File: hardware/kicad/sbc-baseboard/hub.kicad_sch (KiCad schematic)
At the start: 84 parts, among them J1 USB-C upstream, J4 USB-A x2, J5 USB-A x2, U401 USBLC6-2SC6, U402 USB2517, U403 TPS2553DBV, U404 TPS2553DBV, U405 TPS2553DBV, U406 TPS2553DBV, U407 TPS2553DBV, U408 USBLC6-2SC6, U409 USBLC6-2SC6, U410 USBLC6-2SC6, U411 USBLC6-2SC6, Y401 24MHz

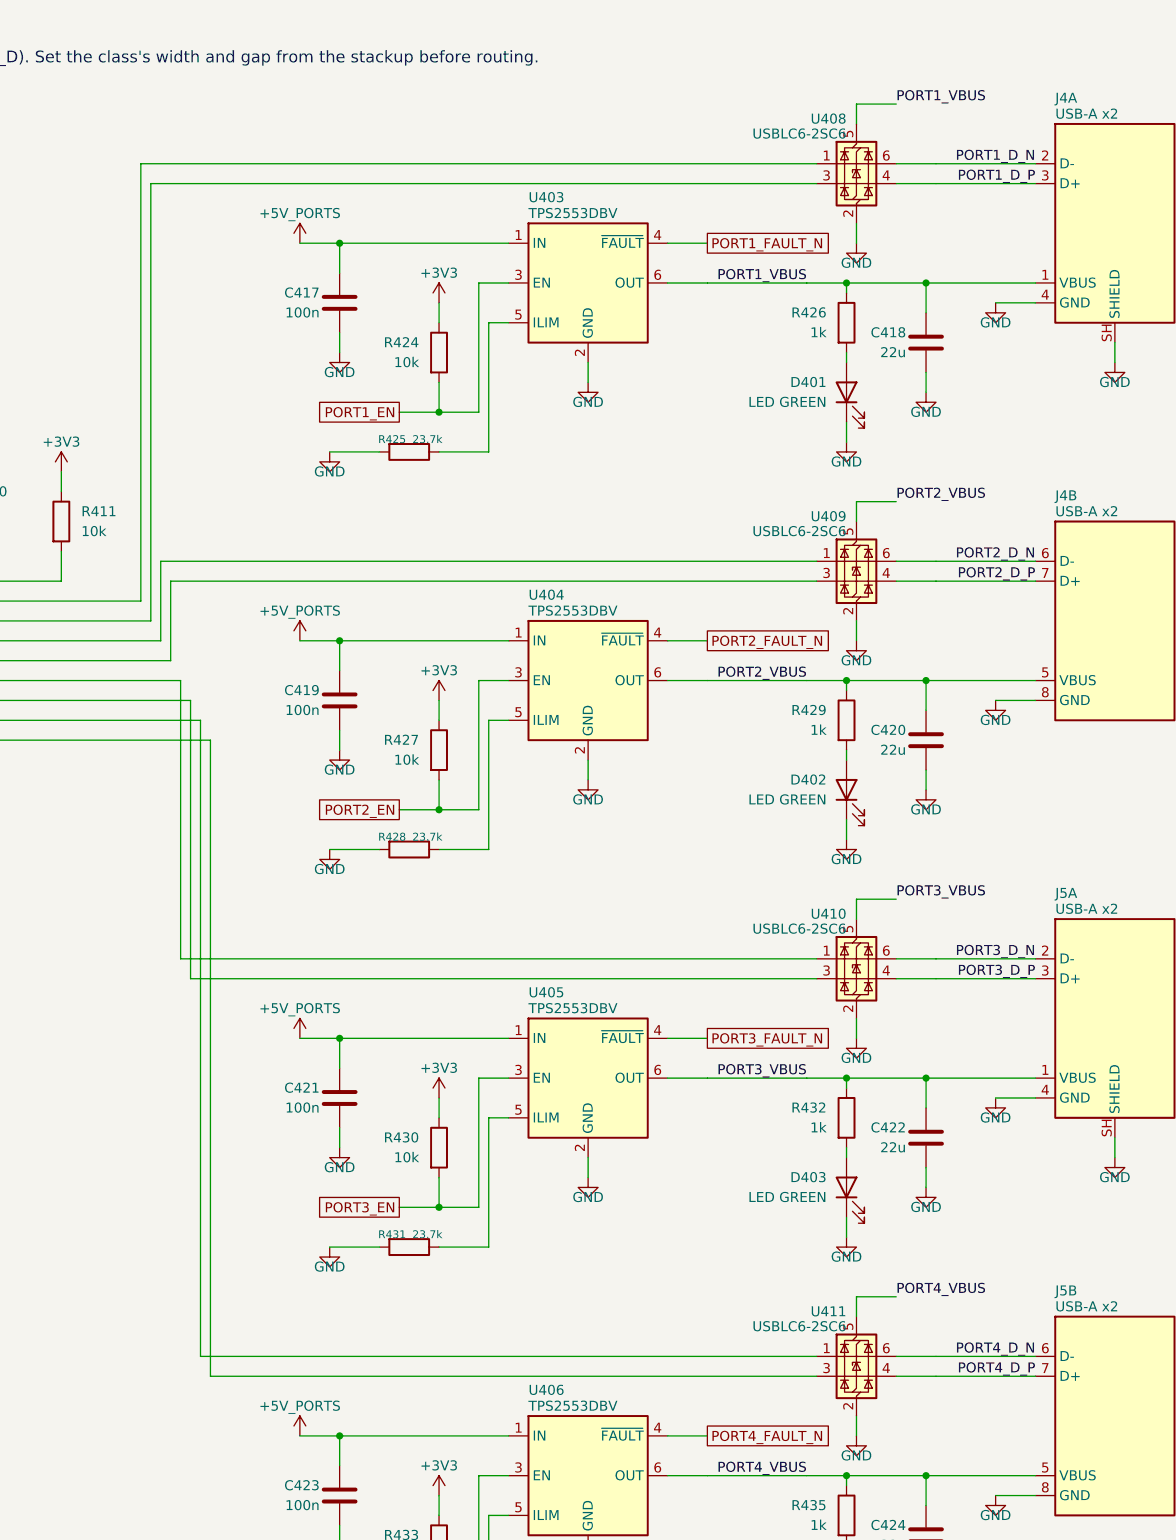
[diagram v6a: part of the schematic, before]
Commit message: Pairs laid as lanes, the rails as L3 regions, the Ethernet pairs named: the board ready for the bulk router
All sixteen USB 2.0 pair segments and the two Ethernet MDI pairs are laid
by the standard's placer from pair lanes in gen/layout.py: members at the
class geometry, escapes at the pads, the USB-C receptacles' doubled pads
bridged behind their rows, two pairs passing under the port pairs on the
bottom, every pair matched to within 0.25 mm, no crossings (the port
arrays and the J3 array use the house symbol drawn with I/O2 on top, the
K64's USB pins wired to its rows). J4 and J5 trade places so each stack's
pairs reach the hub row they are wired to. The ESD arrays, the series
parts and the SWD header are anchored for the lanes. The rails are
regions on In2.Cu at distinct priorities over a 3V3 base. The Ethernet
MDI pairs are named ETH_TD/RD and classed ETH (100 ohm). DRC: the 12
documented errors, no warnings but the unfilled rail islands; 499
connections for the bulk router (gen/pcb.py --route), which is running.

Co-Authored-By: Claude Fable 5.1 <noreply@anthropic.com>
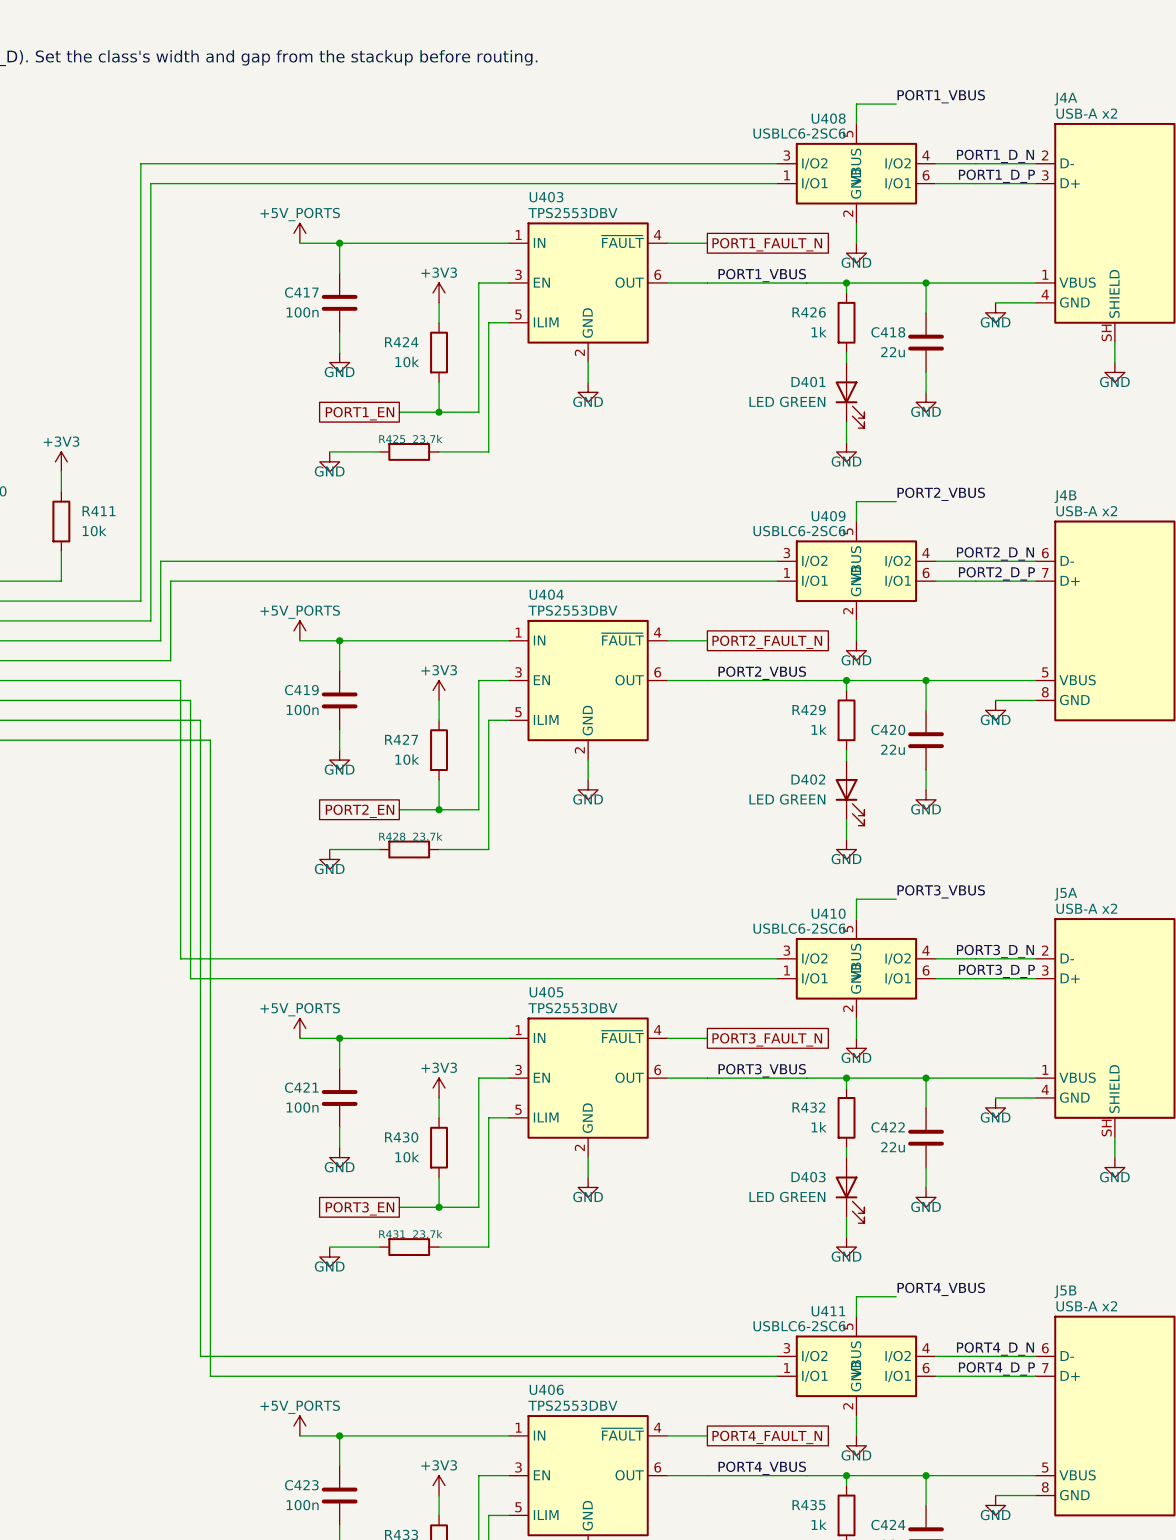
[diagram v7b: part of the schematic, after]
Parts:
- U408, U409, U410, U411: symbol Power_Protection:USBLC6-2SC6 -> calico-ic:USBLC6-2SC6-IO2up
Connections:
- net HUB_DN4_N: now also U408.3 (I/O2); no longer U408.1 (I/O1)
- net HUB_DN4_P: now also U408.1 (I/O1); no longer U408.3 (I/O2)
- net HUB_DN5_N: now also U409.3 (I/O2); no longer U409.1 (I/O1)
- net HUB_DN5_P: now also U409.1 (I/O1); no longer U409.3 (I/O2)
- net HUB_DN6_N: now also U410.3 (I/O2); no longer U410.1 (I/O1)
- net HUB_DN6_P: now also U410.1 (I/O1); no longer U410.3 (I/O2)
- net HUB_DN7_N: now also U411.3 (I/O2); no longer U411.1 (I/O1)
- net HUB_DN7_P: now also U411.1 (I/O1); no longer U411.3 (I/O2)
- net PORT1_D_N: now also U408.4 (I/O2); no longer U408.6 (I/O1)
- net PORT1_D_P: now also U408.6 (I/O1); no longer U408.4 (I/O2)
- net PORT2_D_N: now also U409.4 (I/O2); no longer U409.6 (I/O1)
- net PORT2_D_P: now also U409.6 (I/O1); no longer U409.4 (I/O2)
- net PORT3_D_N: now also U410.4 (I/O2); no longer U410.6 (I/O1)
- net PORT3_D_P: now also U410.6 (I/O1); no longer U410.4 (I/O2)
- net PORT4_D_N: now also U411.4 (I/O2); no longer U411.6 (I/O1)
- net PORT4_D_P: now also U411.6 (I/O1); no longer U411.4 (I/O2)
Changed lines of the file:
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@@
 	)
 	(symbol
-		(lib_id "Power_Protection:USBLC6-2SC6")
-		(at 361.95 45.72 0)
+		(lib_id "calico-ic:USBLC6-2SC6-IO2up")
+		(at 361.95 48.26 0)
 		(unit 1)
 		(body_style 1)
@@
 		)
 		(property "Footprint" "Package_TO_SOT_SMD:SOT-23-6"
-			(at 361.95 45.72 0)
+			(at 361.95 48.26 0)
 			(hide yes)
 			(show_name no)
@@
 		)
 		(property "Datasheet" "~"
-			(at 361.95 45.72 0)
+			(at 361.95 48.26 0)
 			(hide yes)
 			(show_name no)
@@
 			)
 		)
-		(property "Description" "Very low capacitance ESD protection diode, 2 data-line, SOT-23-6"
-			(at 361.95 45.72 0)
+		(property "Description" "USB 2.0 ESD protection array, two flow-through channels, SOT-23-6; drawn with I/O2 on the upper row"
+			(at 361.95 48.26 0)
 			(hide yes)
 			(show_name no)
@@
 			)
 		)
-		(pin "1"
-		)
-		(pin "2"
-		)
 		(pin "3"
 		)
+		(pin "1"
+		)
 		(pin "4"
 		)
+		(pin "6"
+		)
 		(pin "5"
 		)
-		(pin "6"
+		(pin "2"
 		)
 		(instances
@@
 	)
 	(symbol
-		(lib_id "Power_Protection:USBLC6-2SC6")
-		(at 361.95 96.52 0)
+		(lib_id "calico-ic:USBLC6-2SC6-IO2up")
+		(at 361.95 99.06 0)
 		(unit 1)
 		(body_style 1)
@@
 		)
 		(property "Footprint" "Package_TO_SOT_SMD:SOT-23-6"
-			(at 361.95 96.52 0)
+			(at 361.95 99.06 0)
 			(hide yes)
 			(show_name no)
@@
 		)
 		(property "Datasheet" "~"
-			(at 361.95 96.52 0)
+			(at 361.95 99.06 0)
 			(hide yes)
 			(show_name no)
@@
 			)
 		)
-		(property "Description" "Very low capacitance ESD protection diode, 2 data-line, SOT-23-6"
-			(at 361.95 96.52 0)
+		(property "Description" "USB 2.0 ESD protection array, two flow-through channels, SOT-23-6; drawn with I/O2 on the upper row"
+			(at 361.95 99.06 0)
 			(hide yes)
 			(show_name no)
@@
 			)
 		)
-		(pin "1"
-		)
-		(pin "2"
-		)
 		(pin "3"
 		)
+		(pin "1"
+		)
 		(pin "4"
 		)
+		(pin "6"
+		)
 		(pin "5"
 		)
-		(pin "6"
+		(pin "2"
 		)
 		(instances
@@
 	)
 	(symbol
-		(lib_id "Power_Protection:USBLC6-2SC6")
-		(at 361.95 147.32 0)
+		(lib_id "calico-ic:USBLC6-2SC6-IO2up")
+		(at 361.95 149.86 0)
 		(unit 1)
 		(body_style 1)
@@
 		)
 		(property "Footprint" "Package_TO_SOT_SMD:SOT-23-6"
-			(at 361.95 147.32 0)
+			(at 361.95 149.86 0)
 			(hide yes)
 			(show_name no)
@@
 		)
 		(property "Datasheet" "~"
-			(at 361.95 147.32 0)
+			(at 361.95 149.86 0)
 			(hide yes)
 			(show_name no)
@@
 			)
 		)
-		(property "Description" "Very low capacitance ESD protection diode, 2 data-line, SOT-23-6"
-			(at 361.95 147.32 0)
+		(property "Description" "USB 2.0 ESD protection array, two flow-through channels, SOT-23-6; drawn with I/O2 on the upper row"
+			(at 361.95 149.86 0)
 			(hide yes)
 			(show_name no)
@@
 			)
 		)
-		(pin "1"
-		)
-		(pin "2"
-		)
 		(pin "3"
 		)
+		(pin "1"
+		)
 		(pin "4"
 		)
+		(pin "6"
+		)
 		(pin "5"
 		)
-		(pin "6"
+		(pin "2"
 		)
 		(instances
@@
 	)
 	(symbol
-		(lib_id "Power_Protection:USBLC6-2SC6")
-		(at 361.95 198.12 0)
+		(lib_id "calico-ic:USBLC6-2SC6-IO2up")
+		(at 361.95 200.66 0)
 		(unit 1)
 		(body_style 1)
@@
 		)
 		(property "Footprint" "Package_TO_SOT_SMD:SOT-23-6"
-			(at 361.95 198.12 0)
+			(at 361.95 200.66 0)
 			(hide yes)
 			(show_name no)
@@
 		)
 		(property "Datasheet" "~"
-			(at 361.95 198.12 0)
+			(at 361.95 200.66 0)
 			(hide yes)
 			(show_name no)
@@
 			)
 		)
-		(property "Description" "Very low capacitance ESD protection diode, 2 data-line, SOT-23-6"
-			(at 361.95 198.12 0)
+		(property "Description" "USB 2.0 ESD protection array, two flow-through channels, SOT-23-6; drawn with I/O2 on the upper row"
+			(at 361.95 200.66 0)
 			(hide yes)
 			(show_name no)
@@
 			)
 		)
-		(pin "1"
-		)
-		(pin "2"
-		)
 		(pin "3"
 		)
+		(pin "1"
+		)
 		(pin "4"
 		)
+		(pin "6"
+		)
 		(pin "5"
 		)
-		(pin "6"
+		(pin "2"
 		)
 		(instances
@@
 		(pts
 			(xy 270.51 45.72)
-			(xy 356.87 45.72)
+			(xy 351.79 45.72)
 		)
 		(stroke
@@
 		(pts
 			(xy 271.78 48.26)
-			(xy 356.87 48.26)
+			(xy 351.79 48.26)
 		)
 		(stroke
@@
 		(pts
 			(xy 273.05 96.52)
-			(xy 356.87 96.52)
+			(xy 351.79 96.52)
 		)
 		(stroke
@@
 		(pts
 			(xy 274.32 99.06)
-			(xy 356.87 99.06)
+			(xy 351.79 99.06)
 		)
 		(stroke
@@
 		(pts
 			(xy 275.59 147.32)
-			(xy 356.87 147.32)
+			(xy 351.79 147.32)
 		)
 		(stroke
@@
 		(pts
 			(xy 276.86 149.86)
-			(xy 356.87 149.86)
+			(xy 351.79 149.86)
 		)
 		(stroke
@@
 		(pts
 			(xy 278.13 198.12)
-			(xy 356.87 198.12)
+			(xy 351.79 198.12)
 		)
 		(stroke
@@
 		(pts
 			(xy 279.4 200.66)
-			(xy 356.87 200.66)
+			(xy 351.79 200.66)
 		)
 		(stroke
@@
 	(wire
 		(pts
-			(xy 367.03 45.72)
 			(xy 372.11 45.72)
+			(xy 377.19 45.72)
 		)
 		(stroke
@@
 	(wire
 		(pts
-			(xy 372.11 45.72)
+			(xy 377.19 45.72)
 			(xy 384.81 45.72)
 		)
@@
 	(wire
 		(pts
-			(xy 367.03 48.26)
 			(xy 372.11 48.26)
+			(xy 377.19 48.26)
 		)
 		(stroke
@@
 	(wire
 		(pts
-			(xy 372.11 48.26)
+			(xy 377.19 48.26)
 			(xy 384.81 48.26)
 		)
@@
 	(wire
 		(pts
-			(xy 367.03 96.52)
 			(xy 372.11 96.52)
+			(xy 377.19 96.52)
 		)
 		(stroke
@@
 	(wire
 		(pts
-			(xy 372.11 96.52)
+			(xy 377.19 96.52)
 			(xy 384.81 96.52)
 		)
@@
 	(wire
 		(pts
-			(xy 367.03 99.06)
 			(xy 372.11 99.06)
+			(xy 377.19 99.06)
 		)
 		(stroke
@@
 	(wire
 		(pts
-			(xy 372.11 99.06)
+			(xy 377.19 99.06)
 			(xy 384.81 99.06)
 		)
@@
 	(wire
 		(pts
-			(xy 367.03 147.32)
 			(xy 372.11 147.32)
+			(xy 377.19 147.32)
 		)
 		(stroke
@@
 	(wire
 		(pts
-			(xy 372.11 147.32)
+			(xy 377.19 147.32)
 			(xy 384.81 147.32)
 		)
@@
 	(wire
 		(pts
-			(xy 367.03 149.86)
 			(xy 372.11 149.86)
+			(xy 377.19 149.86)
 		)
 		(stroke
@@
 	(wire
 		(pts
-			(xy 372.11 149.86)
+			(xy 377.19 149.86)
 			(xy 384.81 149.86)
 		)
@@
 	(wire
 		(pts
-			(xy 367.03 198.12)
 			(xy 372.11 198.12)
+			(xy 377.19 198.12)
 		)
 		(stroke
@@
 	(wire
 		(pts
-			(xy 372.11 198.12)
+			(xy 377.19 198.12)
 			(xy 384.81 198.12)
 		)
@@
 	(wire
 		(pts
-			(xy 367.03 200.66)
 			(xy 372.11 200.66)
+			(xy 377.19 200.66)
 		)
 		(stroke
@@
 	(wire
 		(pts
-			(xy 372.11 200.66)
+			(xy 377.19 200.66)
 			(xy 384.81 200.66)
 		)

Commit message: The three USB-C receptacles use the house GCT footprint with the peg holes clear of the outer ground pads: DRC at zero errors
gen/kit.py points USBC at calico:USB_C_Receptacle_GCT_USB4105-xx-A_16P_TopMnt_Horizontal_PegClear
(ecad-libraries 0.3.5, submodule bumped): KiCad's footprint rebuilt pad for pad
with A1, A12, B1 and B12 0.1 mm shorter at the peg end, hole to copper 0.29 mm
against the fab's 0.25 mm. Schematic rebuilt (ERC clean, the footprint field on
J1-J3, BOM, PDF), board regenerated with the placement unchanged; the twelve
hole-clearance errors are gone. README and the reference-design review record
the deviation from GCT's drawing.

Co-Authored-By: Claude Fable 5.1 <noreply@anthropic.com>
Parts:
- J1: footprint Connector_USB:USB_C_Receptacle_GCT_USB4105-xx-A_16P_TopMnt_Horizontal -> calico:USB_C_Receptacle_GCT_USB4105-xx-A_16P_TopMnt_Horizontal_PegClear
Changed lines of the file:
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@@
 			)
 		)
-		(property "Footprint" "Connector_USB:USB_C_Receptacle_GCT_USB4105-xx-A_16P_TopMnt_Horizontal"
+		(property "Footprint" "calico:USB_C_Receptacle_GCT_USB4105-xx-A_16P_TopMnt_Horizontal_PegClear"
 			(at 35.56 74.93 0)
 			(hide yes)
